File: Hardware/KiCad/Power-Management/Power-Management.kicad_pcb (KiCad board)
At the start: 2 copper layers, 108 x 67 mm, 52 parts, among them IC1 RT9080-33GJ5, J1 Screw_Terminal_01x02, J2 Conn_01x06, J3 Screw_Terminal_01x02, K1 FINDER-36.11, Q1 BC817, T1 ZMPT101B, U1 STM32F401CCU6, U2 ACS758xCB-050B-PFF, U3 ESP-01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

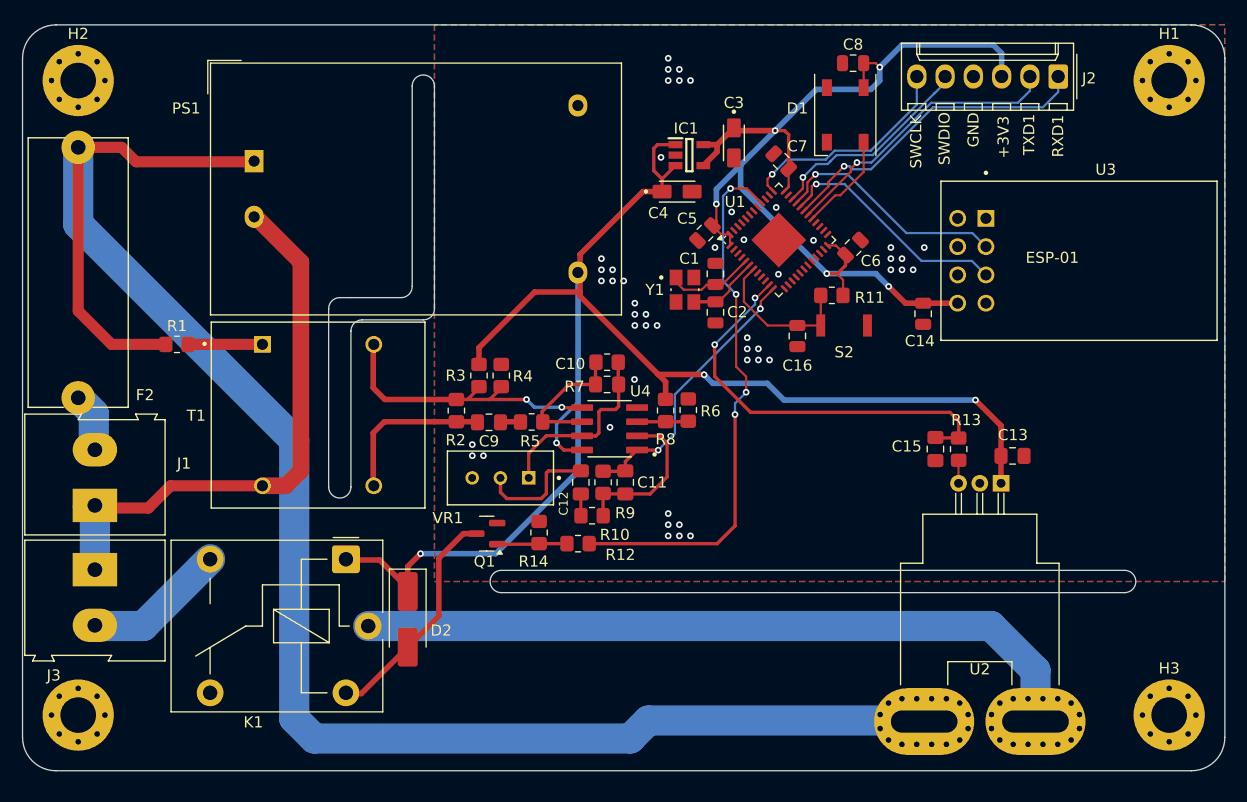
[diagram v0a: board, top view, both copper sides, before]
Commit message: troca de sensor de corrente
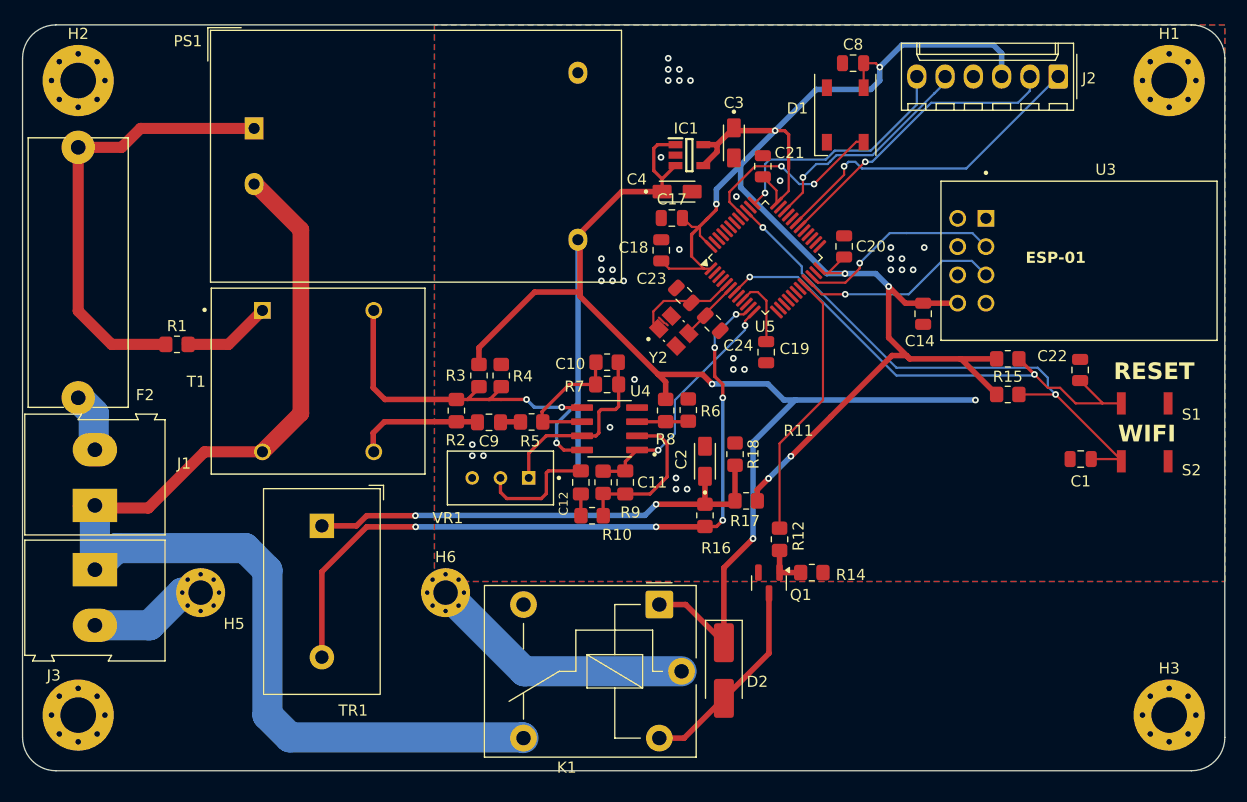
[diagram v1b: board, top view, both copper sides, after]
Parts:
- removed C13: 100nF, Capacitor_SMD:C_0805_2012Metric_Pad1.18x1.45mm_HandSolder
- removed C15: 270nF, Capacitor_SMD:C_0805_2012Metric_Pad1.18x1.45mm_HandSolder
- removed C16, C6: 100nF, Capacitor_SMD:C_0805_2012Metric
- removed C5: 22uF 10V, Capacitor_SMD:C_0805_2012Metric
- removed C7: 10pF, Capacitor_SMD:C_0805_2012Metric
- removed R13: 10K, Resistor_SMD:R_0805_2012Metric_Pad1.20x1.40mm_HandSolder
- removed U1: STM32F401CCU6, Package_DFN_QFN:QFN-48-1EP_7x7mm_P0.5mm_EP3.5x3.5mm
- removed U2: ACS758xCB-050B-PFF, Sensor_Current:Allegro_CB_PFF
- removed Y1: 25Mhz, TSX-3225_25.0000MF10Z-W:XTAL_TSX-3225_25.0000MF10Z-W
- added C17: 100nF, Capacitor_SMD:C_0805_2012Metric, F.Cu at (180.3, 67.3)
- added C18: 100nF, Capacitor_SMD:C_0805_2012Metric, F.Cu at (179.4, 70.2)
- added C19: 10uF, Capacitor_SMD:C_0805_2012Metric, F.Cu at (188.8, 79.4)
- added C20: 100nF, Capacitor_SMD:C_0805_2012Metric, F.Cu at (195.8, 69.9)
- added C21: 100nF, Capacitor_SMD:C_0805_2012Metric, F.Cu at (188.5, 62.7)
- added C22: 100nF, Capacitor_SMD:C_0805_2012Metric, F.Cu at (217.0, 81.0)
- added C23: 10pF, Capacitor_SMD:C_0805_2012Metric, F.Cu at (181.4, 74.3)
- added C24: 10pF, Capacitor_SMD:C_0805_2012Metric, F.Cu at (184.0, 76.8)
- added G***: LOGO, Silkscreen images:Attention_high_voltage, B.Cu at (136.7, 58.0)
- added G***: LOGO, Silkscreen images:Attention_high_voltage, B.Cu at (137.1, 109.0)
- added G***: LOGO, Silkscreen images:Attention_high_voltage, B.Cu at (137.0, 82.0)
- added H5: MountingHole_Pad, MountingHole:MountingHole_2.2mm_M2_Pad_Via, F.Cu at (138.0, 101.0)
- added H6: MountingHole_Pad, MountingHole:MountingHole_2.2mm_M2_Pad_Via, F.Cu at (160.0, 101.0)
- added R15: 10K, Resistor_SMD:R_0805_2012Metric_Pad1.20x1.40mm_HandSolder, F.Cu at (210.5, 80.0)
- added R16: 33, Resistor_SMD:R_0805_2012Metric_Pad1.20x1.40mm_HandSolder, F.Cu at (183.3, 94.1)
- added R17: 100K, Resistor_SMD:R_0805_2012Metric_Pad1.20x1.40mm_HandSolder, F.Cu at (187.0, 92.8)
- added R18: 100K, Resistor_SMD:R_0805_2012Metric_Pad1.20x1.40mm_HandSolder, F.Cu at (186.0, 88.6)
- added S1: SKRKAEE010, SKRKAEE010:SKRK, F.Cu at (222.8, 84.0)
- added TR1: ZMCT103C, Transformer_THT:Transformer_Zeming_ZMCT103C, F.Cu at (148.9, 95.0)
- added U5: STM32F103C8Tx, Package_QFP:LQFP-48_7x7mm_P0.5mm, F.Cu at (188.7, 70.9)
- added Y2: 16Mhz, TSX-3225_25.0000MF10Z-W:XTAL_TSX-3225_25.0000MF10Z-W, F.Cu at (180.5, 77.5)
- C1: value 5pF -> 100nF
- C2: value 10pF -> T491A105M025AG; footprint Capacitor_SMD:C_0805_2012Metric -> T491A105M025AG:CAPMP3216X180N
- moved C1 36.8 mm to (217.1, 89.0), turned to 0 degrees
- moved S2 29.6 mm to (222.8, 89.2)
- moved D2 28.8 mm to (185.0, 108.0)
- moved K1 28.4 mm to (179.2, 102.1)
- moved Q1 25.7 mm to (189.1, 100.1), turned to -90 degrees
- moved R14 24.8 mm to (192.9, 99.2), turned to 180 degrees
- moved R11 18.1 mm to (210.5, 83.2), turned to 0 degrees
- moved R12 18.1 mm to (190.0, 96.2), turned to -90 degrees
- moved C2 13.4 mm to (183.3, 89.2)
- moved T1 3.05 mm to (148.6, 82.0)
- moved PS1 2.94 mm to (142.8, 59.3)
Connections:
- C1 pad 2: Net-(U1-PH0) -> CONFIG_WIFI
- C2 pad 1: GND -> Net-(C2-Pad1)
- C2 pad 2: Net-(U1-PH1) -> GND
- K1 pad 11: F/N-1 | ACS58 -> F/N-1 HOLE
- K1 pad 12: unconnected-(K1-Pad12) -> F/N-2
- K1 pad 14: F/N-1 Borne -> unconnected-(K1-Pad14)
- R11 pad 2: Net-(U1-NRST) -> CONFIG_WIFI
- S2 pad 2: Net-(U1-NRST) -> CONFIG_WIFI
- U3 pad 2: RXD6 -> RXD3
- U3 pad 3: TXD6 -> TXD3
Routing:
- net F/N-1: track 157.2 -> 40.0 mm
- net F/N-1 | ACS58: track 66.2 -> 0.00 mm
- net +3V3: track 92.9 -> 151.5 mm, vias 5 -> 7
- net F/N-2: track 51.5 -> 105.5 mm
- net CONFIG_WIFI: track 0.00 -> 49.9 mm, vias 0 -> 2
- net Net-(U5-NRST): track 0.00 -> 45.0 mm, vias 0 -> 2
- net Net-(C2-Pad1): track 0.00 -> 43.8 mm, vias 0 -> 2
- net PIN_ACS758: track 37.6 -> 67.3 mm, vias 2 -> 6
- net PIN_RELAY: track 48.9 -> 24.2 mm, vias 4 -> 0
- net F/N-1 HOLE: track 0.00 -> 24.1 mm
- net TXD6: track 21.5 -> 0.00 mm, vias 1 -> 0
- net RXD6: track 21.3 -> 0.00 mm, vias 1 -> 0
- net RXD3: track 0.00 -> 18.5 mm, vias 0 -> 1
- net TXD3: track 0.00 -> 18.3 mm, vias 0 -> 1
- net Net-(U1-NRST): track 13.8 -> 0.00 mm
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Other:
- outline, holes or cut-outs redrawn
- board text added: "RESET"
- board text added: "WIFI"
- board text removed: "+3V3"
- board text removed: "GND"
- board text removed: "RXD1"
- board text removed: "SWCLK"
- board text removed: "SWDIO"
- board text removed: "TXD1"

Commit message: refactor: Voltage transformer Op Amp circuit and current transformer circuit.
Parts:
- added REF**: STM32 DEBUG-UART, Silkscreen:STM32 DEBUG-UART, F.Cu at (207.7, 72.2)
- moved U3 36.0 mm to (202.8, 104.4), turned to 180 degrees
- moved R16 22.8 mm to (160.6, 92.3)
- moved J2 21.5 mm to (216.0, 76.2), turned to 90 degrees
- moved R18 20.6 mm to (165.6, 91.6)
- moved R17 20.6 mm to (166.5, 94.5)
- moved C2 20.0 mm to (163.5, 92.2)
- moved C8 16.0 mm to (180.6, 54.5), turned to 90 degrees
- moved C14 14.9 mm to (198.0, 90.0), turned to 180 degrees
- moved R11 11.8 mm to (198.7, 84.0)
- moved R15 11.8 mm to (198.7, 80.8)
- moved D1 10.7 mm to (185.6, 55.2), turned to 0 degrees
- moved H1 10.0 mm to (215.0, 55.0)
- moved H3 10.0 mm to (215.0, 112.0)
- moved C10 9.86 mm to (166.2, 77.0)
- moved R7 9.86 mm to (166.2, 75.0)
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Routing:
- net Net-(C2-Pad1): track 43.8 -> 21.4 mm, vias 2 -> 0
- net +5V: track 137.0 -> 114.9 mm
- net TXD3: track 18.3 -> 32.1 mm
- net RXD3: track 18.5 -> 31.0 mm, vias 1 -> 3
- net Net-(U5-NRST): track 45.0 -> 35.5 mm, vias 2 -> 3
- net +3V3: track 151.5 -> 160.2 mm, vias 7 -> 8
- net Net-(U4-1IN+): track 4.59 -> 11.9 mm, vias 0 -> 2
- net SWCLK: track 22.3 -> 29.3 mm
- net SWDIO: track 20.6 -> 25.9 mm, vias 1 -> 0
- net PIN_ZMPT101B: track 22.2 -> 27.1 mm
- net PIN_LED_RGB: track 17.8 -> 22.1 mm
- net Net-(U4-2OUT): track 17.2 -> 21.5 mm
- net CONFIG_WIFI: track 49.9 -> 45.9 mm, vias 2 -> 4
- net Net-(C12-Pad2): track 10.9 -> 8.31 mm
- net PIN_ACS758: track 67.3 -> 65.3 mm, vias 6 -> 4
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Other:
- board size 108 x 67 mm -> 98 x 67 mm
